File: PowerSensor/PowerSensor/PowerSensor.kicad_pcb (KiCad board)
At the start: 2 copper layers, 35.6 x 22.6 mm, 12 parts, among them J1 Current Sens, J3 BAT+, J4 BAT-, J5 Screw_Terminal_01x04, U1 ACS712ELCTR-20A-T_NRND

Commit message: PCB optimozation
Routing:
- net Battery(-): track 12.7 -> 14.1 mm
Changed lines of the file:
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@@
   (segment (start 104.2 96.94) (end 104.2 90.8) (width 1) (layer "F.Cu") (net 4))
   (segment (start 106.725 90.295) (end 106.725 91.3) (width 1) (layer "F.Cu") (net 4))
-  (segment (start 102.4 102.6) (end 98.32 102.6) (width 2) (layer "F.Cu") (net 5))
+  (segment (start 95.9 102.6) (end 95.8 102.5) (width 2) (layer "F.Cu") (net 5))
+  (segment (start 102.4 102.6) (end 95.9 102.6) (width 2) (layer "F.Cu") (net 5))
   (segment (start 95.8 95) (end 95.8 100.08) (width 2) (layer "F.Cu") (net 5))
-  (segment (start 98.32 102.6) (end 95.8 100.08) (width 2) (layer "F.Cu") (net 5))
+  (segment (start 95.8 102.5) (end 95.8 100.08) (width 2) (layer "F.Cu") (net 5))
   (segment (start 109.8 90) (end 110.095 90.295) (width 0.25) (layer "F.Cu") (net 6))
   (segment (start 115.04 89.44) (end 113.3 87.7) (width 0.25) (layer "F.Cu") (net 6))

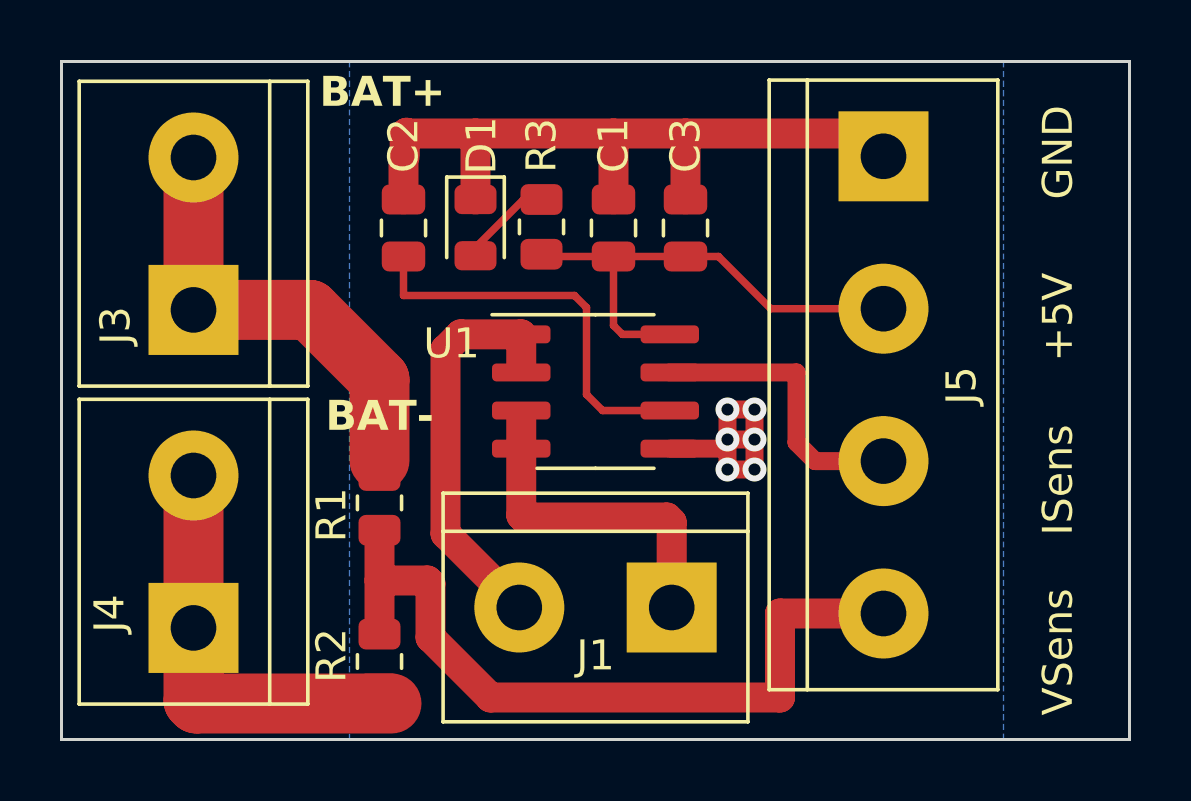
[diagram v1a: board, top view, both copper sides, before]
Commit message: Add the voltage divider into gesgin
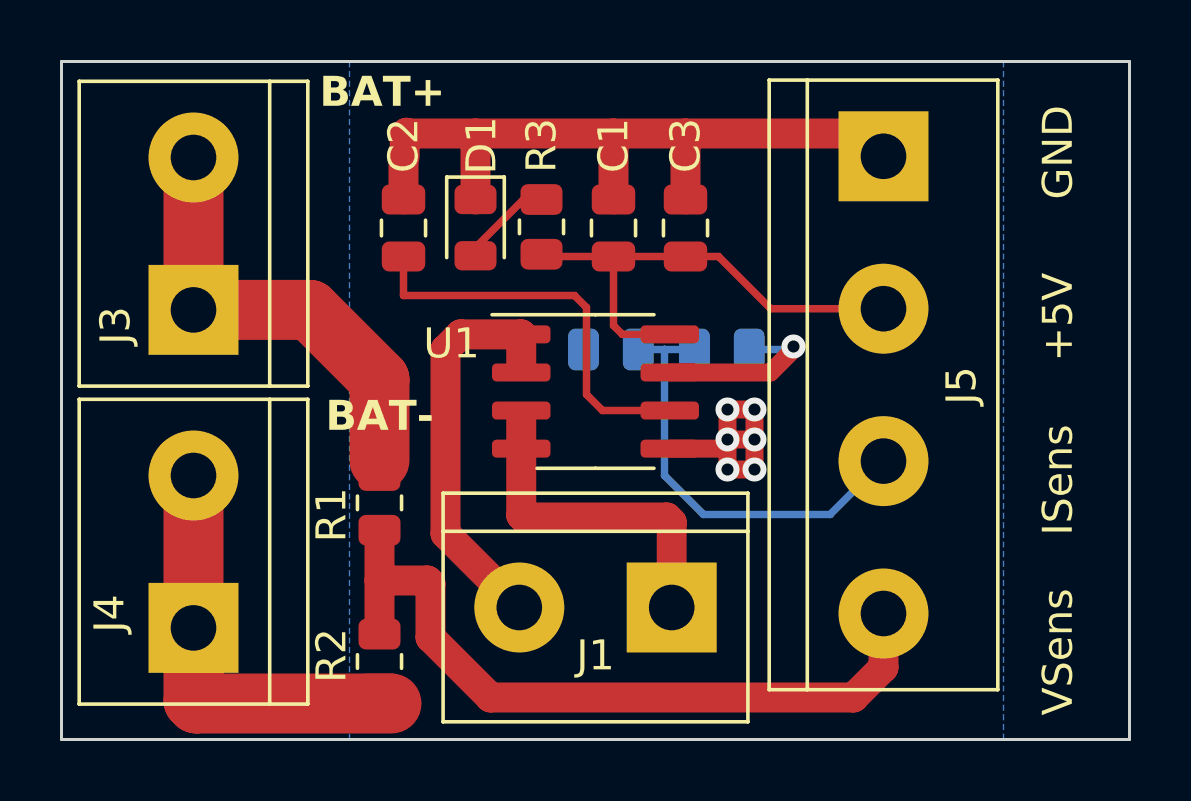
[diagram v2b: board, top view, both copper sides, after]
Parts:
- added R4: 10K, Resistor_SMD:R_0805_2012Metric, B.Cu at (113.4, 90.8)
- added R5: 5K, Resistor_SMD:R_0805_2012Metric, B.Cu at (109.7, 90.8)
- C2: value C -> 1nF
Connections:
- J5 pad 3: VIOUT -> IOut
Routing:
- net IOut: track 0.00 -> 14.7 mm
- net VIOUT: track 9.72 -> 6.30 mm, vias 0 -> 1
- net Vsens: track 25.7 -> 25.1 mm
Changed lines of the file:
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@@
   (net 9 "Battery(+)")
   (net 10 "Net-(U1-FILTER)")
+  (net 11 "IOut")
   (footprint "TerminalBlock:TerminalBlock_bornier-2_P5.08mm" (layer "F.Cu")
     (at 95.8 89.48 90)
@@
         (effects (font (size 1 1) (thickness 0.15)))
     )
-    (fp_text value "C" (at 0 1.68 90) (layer "F.Fab")
+    (fp_text value "1nF" (at 0 1.68 90) (layer "F.Fab")
         (effects (font (size 1 1) (thickness 0.15)))
     )
@@
       (net 6 "+5V") (pinfunction "Pin_2") (pintype "passive"))
     (pad "3" thru_hole circle (at 10.16 0 270) (size 3 3) (drill 1.52) (layers "*.Cu" "*.Mask")
-      (net 7 "VIOUT") (pinfunction "Pin_3") (pintype "passive"))
+      (net 11 "IOut") (pinfunction "Pin_3") (pintype "passive"))
     (pad "4" thru_hole circle (at 15.24 0 270) (size 3 3) (drill 1.52) (layers "*.Cu" "*.Mask")
       (net 8 "Vsens") (pinfunction "Pin_4") (pintype "passive"))
@@
     (pad "2" smd roundrect (at 0.9125 0 90) (size 1.025 1.4) (layers "F.Cu" "F.Paste" "F.Mask") (roundrect_rratio 0.243902)
       (net 2 "Net-(D1-A)") (pintype "passive"))
+    (model "${KICAD6_3DMODEL_DIR}/Resistor_SMD.3dshapes/R_0805_2012Metric.wrl"
+      (offset (xyz 0 0 0))
+      (scale (xyz 1 1 1))
+      (rotate (xyz 0 0 0))
+    )
+  )
+  (footprint "Resistor_SMD:R_0805_2012Metric" (layer "B.Cu")
+    (at 113.4125 90.8 180)
+    (descr "Resistor SMD 0805 (2012 Metric), square (rectangular) end terminal, IPC_7351 nominal, (Body size source: IPC-SM-782 page 72, https://www.pcb-3d.com/wordpress/wp-content/uploads/ipc-sm-782a_amendment_1_and_2.pdf), generated with kicad-footprint-generator")
+    (tags "resistor")
+    (property "Sheetfile" "PowerSensor.kicad_sch")
+    (property "Sheetname" "")
+    (property "ki_description" "Resistor")
+    (property "ki_keywords" "R res resistor")
+    (attr smd)
+    (fp_text reference "R4" (at 0 1.65) (layer "B.SilkS")
+        (effects (font (size 1 1) (thickness 0.15)) (justify mirror))
+    )
+    (fp_text value "10K" (at 0 -1.65) (layer "B.Fab")
+        (effects (font (size 1 1) (thickness 0.15)) (justify mirror))
+    )
+    (fp_text user "${REFERENCE}" (at 0 0) (layer "B.Fab")
+        (effects (font (size 0.5 0.5) (thickness 0.08)) (justify mirror))
+    )
+    (fp_line (start -0.227064 -0.735) (end 0.227064 -0.735)
+      (stroke (width 0.12) (type solid)) (layer "B.SilkS"))
+    (fp_line (start -0.227064 0.735) (end 0.227064 0.735)
+      (stroke (width 0.12) (type solid)) (layer "B.SilkS"))
+    (fp_line (start -1.68 -0.95) (end -1.68 0.95)
+      (stroke (width 0.05) (type solid)) (layer "B.CrtYd"))
+    (fp_line (start -1.68 0.95) (end 1.68 0.95)
+      (stroke (width 0.05) (type solid)) (layer "B.CrtYd"))
+    (fp_line (start 1.68 -0.95) (end -1.68 -0.95)
+      (stroke (width 0.05) (type solid)) (layer "B.CrtYd"))
+    (fp_line (start 1.68 0.95) (end 1.68 -0.95)
+      (stroke (width 0.05) (type solid)) (layer "B.CrtYd"))
+    (fp_line (start -1 -0.625) (end -1 0.625)
+      (stroke (width 0.1) (type solid)) (layer "B.Fab"))
+    (fp_line (start -1 0.625) (end 1 0.625)
+      (stroke (width 0.1) (type solid)) (layer "B.Fab"))
+    (fp_line (start 1 -0.625) (end -1 -0.625)
+      (stroke (width 0.1) (type solid)) (layer "B.Fab"))
+    (fp_line (start 1 0.625) (end 1 -0.625)
+      (stroke (width 0.1) (type solid)) (layer "B.Fab"))
+    (pad "1" smd roundrect (at -0.9125 0 180) (size 1.025 1.4) (layers "B.Cu" "B.Paste" "B.Mask") (roundrect_rratio 0.243902)
+      (net 7 "VIOUT") (pintype "passive"))
+    (pad "2" smd roundrect (at 0.9125 0 180) (size 1.025 1.4) (layers "B.Cu" "B.Paste" "B.Mask") (roundrect_rratio 0.243902)
+      (net 11 "IOut") (pintype "passive"))
+    (model "${KICAD6_3DMODEL_DIR}/Resistor_SMD.3dshapes/R_0805_2012Metric.wrl"
+      (offset (xyz 0 0 0))
+      (scale (xyz 1 1 1))
+      (rotate (xyz 0 0 0))
+    )
+  )
+  (footprint "Resistor_SMD:R_0805_2012Metric" (layer "B.Cu")
+    (at 109.7125 90.8 180)
+    (descr "Resistor SMD 0805 (2012 Metric), square (rectangular) end terminal, IPC_7351 nominal, (Body size source: IPC-SM-782 page 72, https://www.pcb-3d.com/wordpress/wp-content/uploads/ipc-sm-782a_amendment_1_and_2.pdf), generated with kicad-footprint-generator")
+    (tags "resistor")
+    (property "Sheetfile" "PowerSensor.kicad_sch")
+    (property "Sheetname" "")
+    (property "ki_description" "Resistor")
+    (property "ki_keywords" "R res resistor")
+    (attr smd)
+    (fp_text reference "R5" (at 0 1.65) (layer "B.SilkS")
+        (effects (font (size 1 1) (thickness 0.15)) (justify mirror))
+    )
+    (fp_text value "5K" (at 0 -1.65) (layer "B.Fab")
+        (effects (font (size 1 1) (thickness 0.15)) (justify mirror))
+    )
+    (fp_text user "${REFERENCE}" (at 0 0) (layer "B.Fab")
+        (effects (font (size 0.5 0.5) (thickness 0.08)) (justify mirror))
+    )
+    (fp_line (start -0.227064 -0.735) (end 0.227064 -0.735)
+      (stroke (width 0.12) (type solid)) (layer "B.SilkS"))
+    (fp_line (start -0.227064 0.735) (end 0.227064 0.735)
+      (stroke (width 0.12) (type solid)) (layer "B.SilkS"))
+    (fp_line (start -1.68 -0.95) (end -1.68 0.95)
+      (stroke (width 0.05) (type solid)) (layer "B.CrtYd"))
+    (fp_line (start -1.68 0.95) (end 1.68 0.95)
+      (stroke (width 0.05) (type solid)) (layer "B.CrtYd"))
+    (fp_line (start 1.68 -0.95) (end -1.68 -0.95)
+      (stroke (width 0.05) (type solid)) (layer "B.CrtYd"))
+    (fp_line (start 1.68 0.95) (end 1.68 -0.95)
+      (stroke (width 0.05) (type solid)) (layer "B.CrtYd"))
+    (fp_line (start -1 -0.625) (end -1 0.625)
+      (stroke (width 0.1) (type solid)) (layer "B.Fab"))
+    (fp_line (start -1 0.625) (end 1 0.625)
+      (stroke (width 0.1) (type solid)) (layer "B.Fab"))
+    (fp_line (start 1 -0.625) (end -1 -0.625)
+      (stroke (width 0.1) (type solid)) (layer "B.Fab"))
+    (fp_line (start 1 0.625) (end 1 -0.625)
+      (stroke (width 0.1) (type solid)) (layer "B.Fab"))
+    (pad "1" smd roundrect (at -0.9125 0 180) (size 1.025 1.4) (layers "B.Cu" "B.Paste" "B.Mask") (roundrect_rratio 0.243902)
+      (net 11 "IOut") (pintype "passive"))
+    (pad "2" smd roundrect (at 0.9125 0 180) (size 1.025 1.4) (layers "B.Cu" "B.Paste" "B.Mask") (roundrect_rratio 0.243902)
+      (net 1 "GND") (pintype "passive"))
     (model "${KICAD6_3DMODEL_DIR}/Resistor_SMD.3dshapes/R_0805_2012Metric.wrl"
       (offset (xyz 0 0 0))
@@
   (segment (start 112.2 87.7) (end 109.8 87.7) (width 0.25) (layer "F.Cu") (net 6))
   (segment (start 109.8 87.7) (end 109.8 90) (width 0.25) (layer "F.Cu") (net 6))
-  (segment (start 115.9 91.565) (end 115.9 93.9) (width 0.6) (layer "F.Cu") (net 7))
-  (segment (start 115.9 93.9) (end 116.52 94.52) (width 0.6) (layer "F.Cu") (net 7))
-  (segment (start 111.675 91.565) (end 115.9 91.565) (width 0.6) (layer "F.Cu") (net 7))
-  (segment (start 116.52 94.52) (end 118.8 94.52) (width 0.6) (layer "F.Cu") (net 7))
-  (segment (start 115.35 99.6) (end 118.8 99.6) (width 1) (layer "F.Cu") (net 8))
-  (segment (start 105.7 102.4) (end 115.35 102.4) (width 1) (layer "F.Cu") (net 8))
-  (segment (start 115.35 102.4) (end 115.35 99.6) (width 1) (layer "F.Cu") (net 8))
+  (segment (start 115.8 90.7) (end 115.9 90.7) (width 0.6) (layer "F.Cu") (net 7))
+  (segment (start 115.035 91.565) (end 115.8 90.8) (width 0.6) (layer "F.Cu") (net 7))
+  (segment (start 115.9 90.7) (end 115.8 90.8) (width 0.6) (layer "F.Cu") (net 7))
+  (segment (start 111.675 91.565) (end 115.035 91.565) (width 0.6) (layer "F.Cu") (net 7))
+  (segment (start 115.8 90.8) (end 115.8 90.7) (width 0.6) (layer "F.Cu") (net 7))
+  (via (at 115.8 90.7) (size 0.8) (drill 0.4) (layers "F.Cu" "B.Cu") (net 7))
+  (segment (start 114.325 90.8) (end 115.7 90.8) (width 0.25) (layer "B.Cu") (net 7))
+  (segment (start 115.7 90.8) (end 115.8 90.7) (width 0.25) (layer "B.Cu") (net 7))
+  (segment (start 105.7 102.4) (end 117.8 102.4) (width 1) (layer "F.Cu") (net 8))
+  (segment (start 103.7 98.6) (end 103.7 100.4) (width 1) (layer "F.Cu") (net 8))
+  (segment (start 103.7 100.4) (end 105.7 102.4) (width 1) (layer "F.Cu") (net 8))
+  (segment (start 102 98.5) (end 103.6 98.5) (width 1) (layer "F.Cu") (net 8))
+  (segment (start 117.8 102.4) (end 118.8 101.4) (width 1) (layer "F.Cu") (net 8))
+  (segment (start 102 96.825) (end 102 100.2875) (width 1) (layer "F.Cu") (net 8))
   (segment (start 103.6 98.5) (end 103.7 98.6) (width 1) (layer "F.Cu") (net 8))
-  (segment (start 103.7 98.6) (end 103.7 100.4) (width 1) (layer "F.Cu") (net 8))
-  (segment (start 102 96.825) (end 102 100.2875) (width 1) (layer "F.Cu") (net 8))
-  (segment (start 102 98.5) (end 103.6 98.5) (width 1) (layer "F.Cu") (net 8))
-  (segment (start 103.7 100.4) (end 105.7 102.4) (width 1) (layer "F.Cu") (net 8))
+  (segment (start 118.8 101.4) (end 118.8 99.6) (width 1) (layer "F.Cu") (net 8))
   (segment (start 95.8 84.4) (end 95.8 89.48) (width 2) (layer "F.Cu") (net 9))
   (segment (start 99.68 89.48) (end 95.8 89.48) (width 2) (layer "F.Cu") (net 9))
@@
   (segment (start 102.8 87.7) (end 102.8 89) (width 0.25) (layer "F.Cu") (net 10))
   (segment (start 108.9 92.3) (end 109.435 92.835) (width 0.25) (layer "F.Cu") (net 10))
+  (segment (start 111.5 95) (end 112.8 96.3) (width 0.25) (layer "B.Cu") (net 11))
+  (segment (start 111.5 90.8) (end 110.625 90.8) (width 0.25) (layer "B.Cu") (net 11))
+  (segment (start 117.02 96.3) (end 118.8 94.52) (width 0.25) (layer "B.Cu") (net 11))
+  (segment (start 112.8 96.3) (end 117.02 96.3) (width 0.25) (layer "B.Cu") (net 11))
+  (segment (start 112.5 90.8) (end 111.5 90.8) (width 0.25) (layer "B.Cu") (net 11))
+  (segment (start 111.5 90.8) (end 111.5 95) (width 0.25) (layer "B.Cu") (net 11))
   (zone (net 1) (net_name "GND") (layer "B.Cu") (hatch edge 0.5)
     (connect_pads yes (clearance 0.5))

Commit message: Optimize the desgin
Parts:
- moved R4 0.80 mm to (113.4, 90.0)
- moved R5 0.80 mm to (109.7, 90.0)
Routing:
- net IOut: track 14.7 -> 12.5 mm
- net GND: track 33.8 -> 35.8 mm
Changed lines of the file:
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@@
   )
   (footprint "Resistor_SMD:R_0805_2012Metric" (layer "B.Cu")
-    (at 113.4125 90.8 180)
+    (at 113.4125 90 180)
     (descr "Resistor SMD 0805 (2012 Metric), square (rectangular) end terminal, IPC_7351 nominal, (Body size source: IPC-SM-782 page 72, https://www.pcb-3d.com/wordpress/wp-content/uploads/ipc-sm-782a_amendment_1_and_2.pdf), generated with kicad-footprint-generator")
     (tags "resistor")
@@
   )
   (footprint "Resistor_SMD:R_0805_2012Metric" (layer "B.Cu")
-    (at 109.7125 90.8 180)
+    (at 109.7125 90 180)
     (descr "Resistor SMD 0805 (2012 Metric), square (rectangular) end terminal, IPC_7351 nominal, (Body size source: IPC-SM-782 page 72, https://www.pcb-3d.com/wordpress/wp-content/uploads/ipc-sm-782a_amendment_1_and_2.pdf), generated with kicad-footprint-generator")
     (tags "resistor")
@@
   (segment (start 102.9 83.575) (end 102.84 83.635) (width 1) (layer "F.Cu") (net 1))
   (segment (start 111.675 94.105) (end 113.295 94.105) (width 0.6) (layer "F.Cu") (net 1))
-  (segment (start 113.6 94.8) (end 114.5 94.8) (width 0.6) (layer "F.Cu") (net 1))
+  (segment (start 114 92.8) (end 113.6 92.8) (width 0.6) (layer "F.Cu") (net 1))
   (segment (start 105.2 85.8) (end 105.2 83.6) (width 1) (layer "F.Cu") (net 1))
   (segment (start 113.295 94.105) (end 113.6 93.8) (width 0.25) (layer "F.Cu") (net 1))
+  (segment (start 114.5 92.8) (end 114 92.8) (width 0.6) (layer "F.Cu") (net 1))
   (segment (start 118.8 84.36) (end 118.04 83.6) (width 1) (layer "F.Cu") (net 1))
   (segment (start 102.84 84.36) (end 102.8 84.4) (width 0.25) (layer "F.Cu") (net 1))
   (segment (start 113.6 93.8) (end 114.5 93.8) (width 0.6) (layer "F.Cu") (net 1))
-  (segment (start 114.5 92.8) (end 113.6 92.8) (width 0.6) (layer "F.Cu") (net 1))
+  (segment (start 114 94.8) (end 114 92.8) (width 0.6) (layer "F.Cu") (net 1))
   (segment (start 112.2 85.8) (end 112.2 83.6) (width 1) (layer "F.Cu") (net 1))
+  (segment (start 114 94.8) (end 114.5 94.8) (width 0.6) (layer "F.Cu") (net 1))
   (segment (start 102.925 83.6) (end 102.9 83.575) (width 1) (layer "F.Cu") (net 1))
   (segment (start 102.8 84.4) (end 102.8 85.8) (width 1) (layer "F.Cu") (net 1))
@@
   (segment (start 109.8 85.8) (end 109.8 83.6) (width 1) (layer "F.Cu") (net 1))
   (segment (start 102.84 83.635) (end 102.84 84.36) (width 1) (layer "F.Cu") (net 1))
+  (segment (start 113.6 94.8) (end 114 94.8) (width 0.6) (layer "F.Cu") (net 1))
   (via (at 113.6 93.8) (size 0.8) (drill 0.4) (layers "F.Cu" "B.Cu") (free) (net 1))
   (via (at 114.5 93.8) (size 0.8) (drill 0.4) (layers "F.Cu" "B.Cu") (free) (net 1))
@@
   (segment (start 115.8 90.8) (end 115.8 90.7) (width 0.6) (layer "F.Cu") (net 7))
   (via (at 115.8 90.7) (size 0.8) (drill 0.4) (layers "F.Cu" "B.Cu") (net 7))
-  (segment (start 114.325 90.8) (end 115.7 90.8) (width 0.25) (layer "B.Cu") (net 7))
+  (segment (start 115.1 90) (end 115.8 90.7) (width 0.25) (layer "B.Cu") (net 7))
+  (segment (start 114.325 90) (end 115.1 90) (width 0.25) (layer "B.Cu") (net 7))
   (segment (start 115.7 90.8) (end 115.8 90.7) (width 0.25) (layer "B.Cu") (net 7))
   (segment (start 105.7 102.4) (end 117.8 102.4) (width 1) (layer "F.Cu") (net 8))
@@
   (segment (start 102.8 87.7) (end 102.8 89) (width 0.25) (layer "F.Cu") (net 10))
   (segment (start 108.9 92.3) (end 109.435 92.835) (width 0.25) (layer "F.Cu") (net 10))
-  (segment (start 111.5 95) (end 112.8 96.3) (width 0.25) (layer "B.Cu") (net 11))
-  (segment (start 111.5 90.8) (end 110.625 90.8) (width 0.25) (layer "B.Cu") (net 11))
-  (segment (start 117.02 96.3) (end 118.8 94.52) (width 0.25) (layer "B.Cu") (net 11))
-  (segment (start 112.8 96.3) (end 117.02 96.3) (width 0.25) (layer "B.Cu") (net 11))
-  (segment (start 112.5 90.8) (end 111.5 90.8) (width 0.25) (layer "B.Cu") (net 11))
-  (segment (start 111.5 90.8) (end 111.5 95) (width 0.25) (layer "B.Cu") (net 11))
+  (segment (start 111.6 91.4) (end 112 91.8) (width 0.25) (layer "B.Cu") (net 11))
+  (segment (start 116.1 92.7) (end 116.1 94) (width 0.25) (layer "B.Cu") (net 11))
+  (segment (start 115.2 91.8) (end 116.1 92.7) (width 0.25) (layer "B.Cu") (net 11))
+  (segment (start 116.62 94.52) (end 118.8 94.52) (width 0.25) (layer "B.Cu") (net 11))
+  (segment (start 112 91.8) (end 115.2 91.8) (width 0.25) (layer "B.Cu") (net 11))
+  (segment (start 116.1 94) (end 116.62 94.52) (width 0.25) (layer "B.Cu") (net 11))
+  (segment (start 111.6 90) (end 112.5 90) (width 0.25) (layer "B.Cu") (net 11))
+  (segment (start 110.625 90) (end 111.6 90) (width 0.25) (layer "B.Cu") (net 11))
+  (segment (start 111.6 90) (end 111.6 91.4) (width 0.25) (layer "B.Cu") (net 11))
   (zone (net 1) (net_name "GND") (layer "B.Cu") (hatch edge 0.5)
     (connect_pads yes (clearance 0.5))
